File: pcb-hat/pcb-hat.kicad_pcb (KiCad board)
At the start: 4 copper layers, 40.9 x 60.1 mm, 67 parts, among them Q1 Q_PMOS_GSD, Q2 Q_NPN, Q3 PJA3404A_R1_00001, U1 Headers, U2 INA219AxD, U3 HTD Servo, U4 TL431DBZ, U5 AP63301WU-7, U7 AP63301WU-7, U8 Raspberry_Pi_Generic

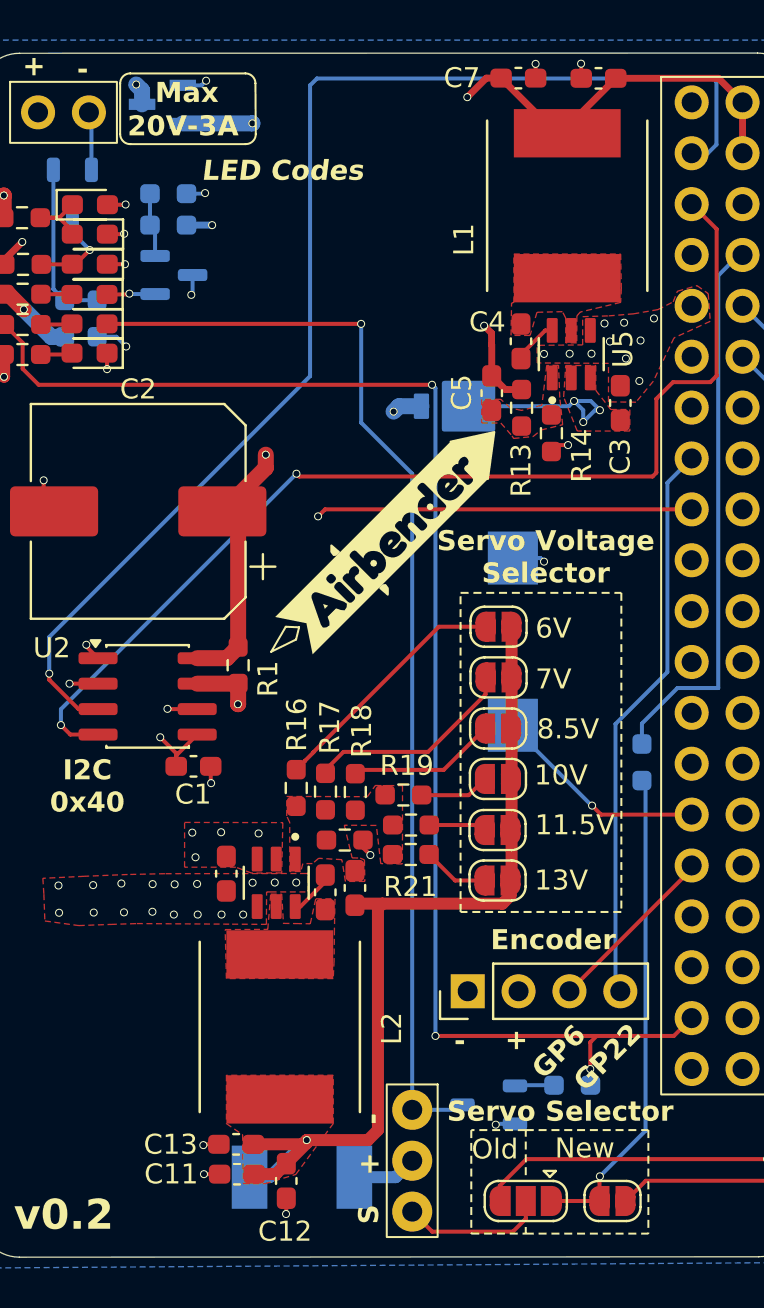
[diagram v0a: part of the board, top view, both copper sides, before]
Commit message: Add digikey pn's to caps and resistors, order board
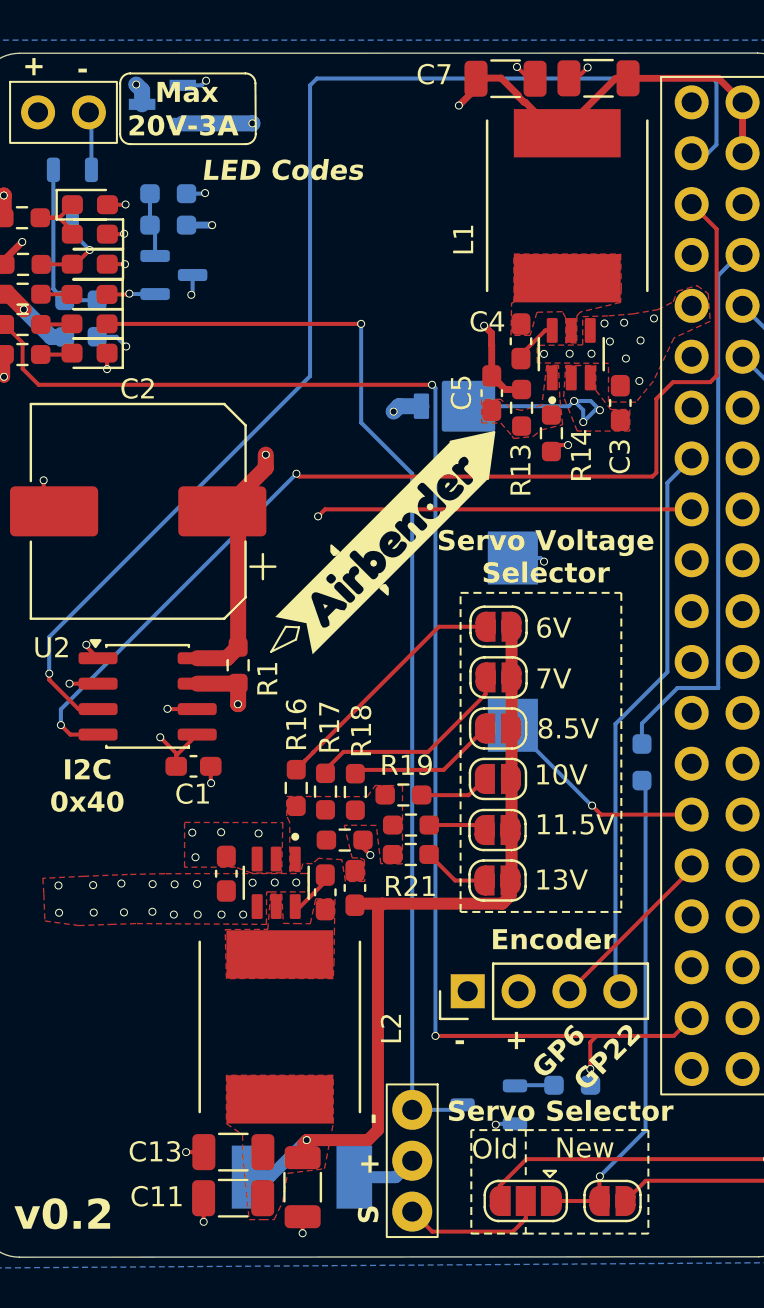
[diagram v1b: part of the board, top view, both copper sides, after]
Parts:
- C11, C12, C13, C6, C7: footprint Capacitor_SMD:C_0603_1608Metric_Pad1.08x0.95mm_HandSolder -> Capacitor_SMD:C_1206_3216Metric
- R17: value 233k -> 232k
- R19: value 346k -> 348k
- R20: value 403k -> 402k
- moved C11 1.21 mm to (123.8, 120.2)
- moved C12 0.87 mm to (127.3, 119.6)
- moved C7 0.64 mm to (137.4, 64.3)
- moved C13 0.41 mm to (123.8, 117.9)
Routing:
- net VDC: track 98.5 -> 92.8 mm
- net GND: track 24.6 -> 26.8 mm

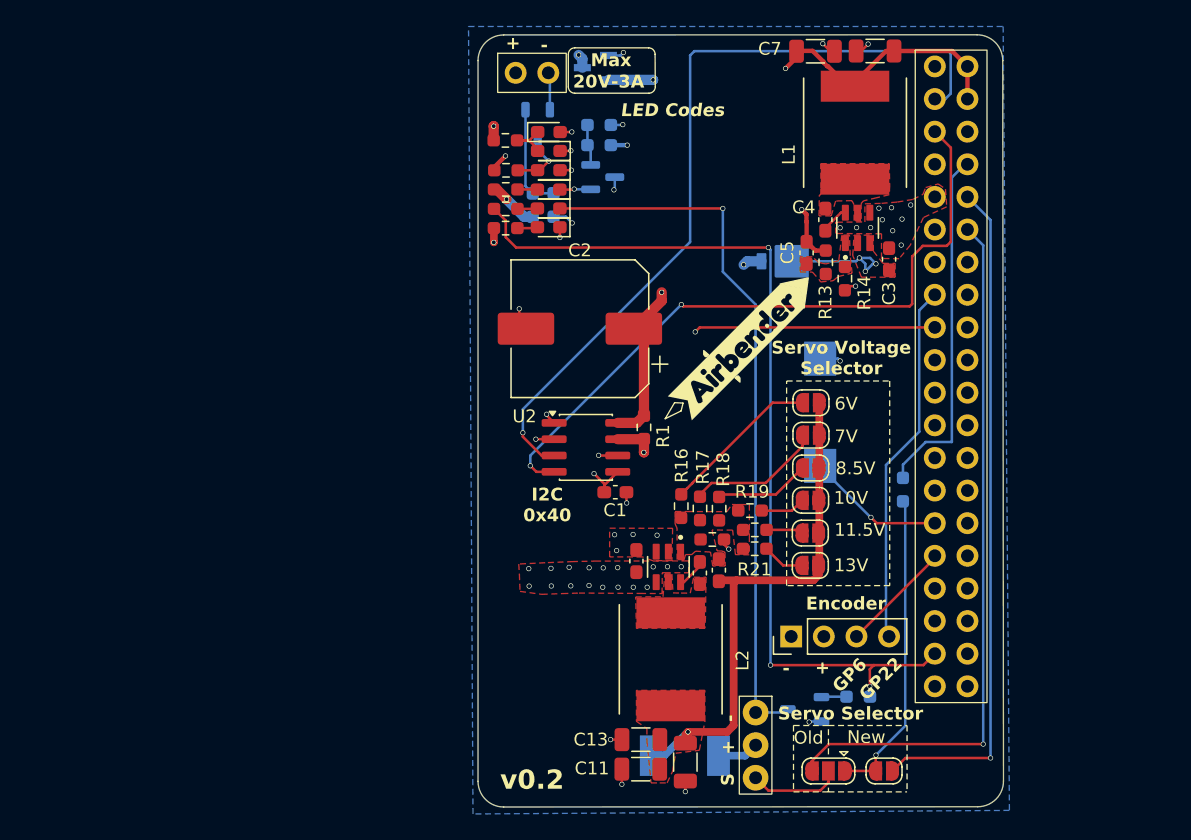
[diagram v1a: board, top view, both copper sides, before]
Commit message: Fix servo RP detection circuit
Start work on routing
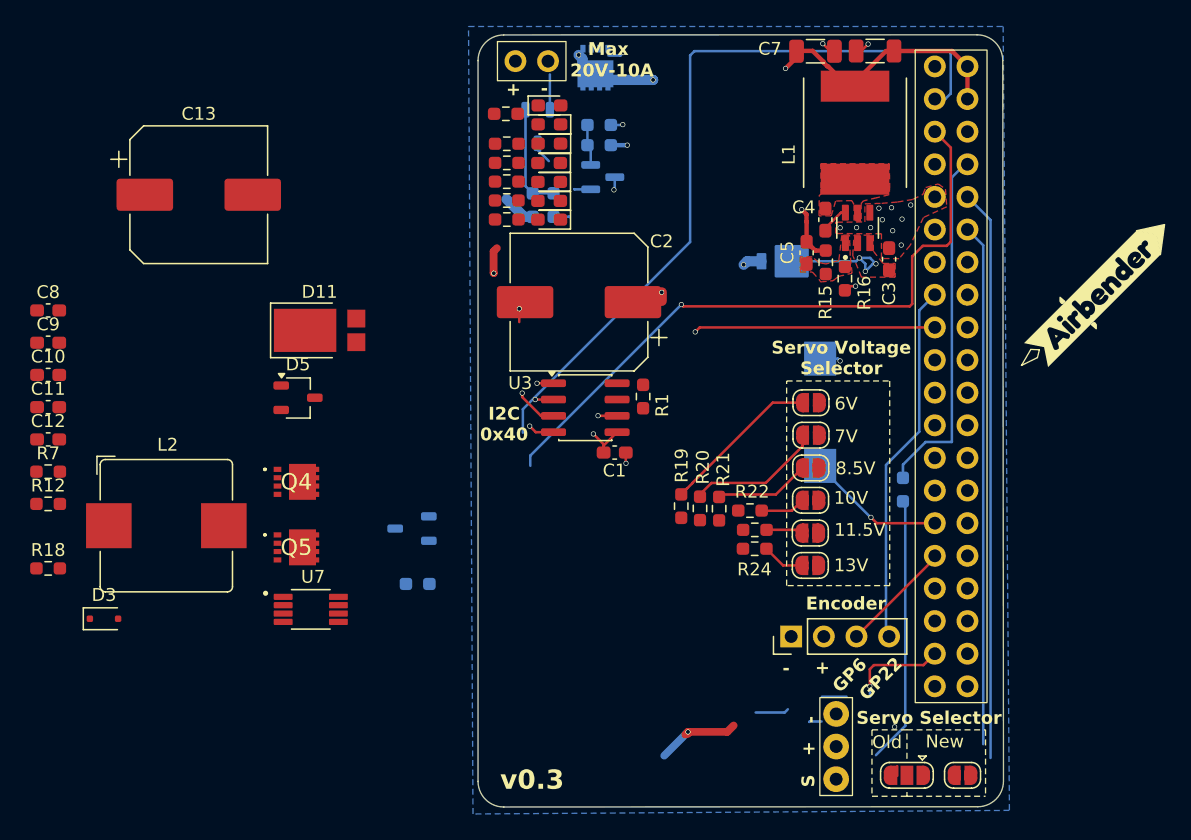
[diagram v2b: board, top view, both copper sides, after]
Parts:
- removed F1: 1812L110_24DR, pcb_hat:FUSM4632X200N
- removed the R15 at (129.4, 102.3)
- added D10: LED_Small, LED_SMD:LED_0603_1608Metric_Pad1.05x0.95mm_HandSolder, F.Cu at (116.7, 75.9)
- added D11: Schottky, Diode_SMD:D_PowerDI-5, F.Cu at (98.8, 86.0)
- added D3: TVS Diode, Diode_SMD:D_SOD-323F, F.Cu at (82.0, 108.5)
- added D5: Zener diode, Package_TO_SOT_SMD:TSOT-23, F.Cu at (97.1, 91.3)
- added Q4: Q_PMOS_GSD, pcb_hat:PJQ4465APAU_R2_000A1, F.Cu at (97.0, 97.8)
- added Q5: Q_PMOS_GSD, pcb_hat:PJQ4465APAU_R2_000A1, F.Cu at (97.0, 102.9)
- added R12: 10k, Resistor_SMD:R_0603_1608Metric_Pad0.98x0.95mm_HandSolder, F.Cu at (77.7, 99.5)
- added R17: 1k, Resistor_SMD:R_0603_1608Metric_Pad0.98x0.95mm_HandSolder, F.Cu at (113.4, 75.9)
- added R18: 49.9k, Resistor_SMD:R_0603_1608Metric_Pad0.98x0.95mm_HandSolder, F.Cu at (77.7, 104.5)
- added R7: 1k, Resistor_SMD:R_0603_1608Metric_Pad0.98x0.95mm_HandSolder, F.Cu at (77.7, 97.0)
- C10: value 12p -> 22u
- C11: value 22u -> 100p; footprint Capacitor_SMD:C_1206_3216Metric -> Capacitor_SMD:C_0603_1608Metric_Pad1.08x0.95mm_HandSolder
- C12: footprint Capacitor_SMD:C_1206_3216Metric -> Capacitor_SMD:C_0603_1608Metric_Pad1.08x0.95mm_HandSolder
- C13: value 22u -> 1000u; footprint Capacitor_SMD:C_1206_3216Metric -> Capacitor_SMD:CP_Elec_10x10.5
- C9: value 100n -> 22u
- L2: value 6.8u -> 4.7u; footprint pcb_hat:IND_ETQP4M6R8KVK -> Inductor_SMD:L_Bourns_SRP1038C_10.0x10.0mm
- Q1: footprint pcb_hat:SOT_7DS-T1-GE3_VIS -> pcb_hat:PJQ4465APAU_R2_000A1
- R14: renamed from R11; value 1k -> 2k
- R19: renamed from R16; value 196k -> 13k
- R20: renamed from R17; value 232k -> 10.7k
- R21: renamed from R18; value 290k -> 8.45k
- R22: renamed from R19; value 348k -> 6.98k
- R23: renamed from R20; value 402k -> 6.04k
- R24: renamed from R21; value 459k -> 5.23k
- R3: renamed from R6; value 4k7 -> 2k
- U7: value AP63301WU-7 -> LM3489; footprint pcb_hat:SOT95P280X100-6N -> pcb_hat:SOP65P490X110-8N
- moved C12 55.6 mm to (77.7, 94.5), turned to 0 degrees
- moved C13 54.6 mm to (89.4, 75.5), turned to 0 degrees
- moved C10 54.4 mm to (77.7, 89.5), turned to 0 degrees
- moved C11 54.1 mm to (77.7, 92.0), turned to 0 degrees
- moved C9 53.8 mm to (77.7, 87.0), turned to 0 degrees
- moved C8 49.8 mm to (77.7, 84.5), turned to 0 degrees
- moved L2 40.6 mm to (86.9, 101.2), turned to 0 degrees
- moved R8 35.4 mm to (106.5, 105.8)
- moved Q3 33.7 mm to (106.0, 101.4)
- moved kibuzzard-694E41B7 28.0 mm to (159.3, 83.2)
- moved U7 28.0 mm to (98.1, 107.7), turned to 0 degrees
- moved U2 6.27 mm to (139.0, 118.4)
- moved JP1 6.12 mm to (148.9, 120.7)
- moved JP2 6.12 mm to (144.5, 120.7)
- moved C1 3.09 mm to (121.8, 95.5)
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- renumbered D3 to D4, D4 to D6, D5 to D7, D7 to D9, R9 to R10, R10 to R11, R12 to R13, R13 to R15, R14 to R16, R3 to R4, R4 to R5, R5 to R6, R7 to R8, R8 to R9, U3 to U2, U2 to U3
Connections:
- net /Pi_RX_Out renamed /PI_RX_OUT
- net /Pi_SCL renamed /PI_SCL
- net /Pi_SDA renamed /PI_SDA
- net /Pi_TX_Out renamed /PI_TX_OUT
- C10 pad 1: VDC -> VCC_LOAD
- C10 pad 2: /V_Choose -> GND
- C11 pad 2: GND -> /V_CHOOSE
- C9 pad 1: Net-(U7-BST) -> VCC_LOAD
- C9 pad 2: Net-(U7-SW) -> GND
- D9 pad 1: /Servo_Control -> GND
- JP2 pad 2: Net-(JP2-C) -> /PI_SIGNAL
- JP3 pad 2: VDC -> GND
- JP4 pad 2: VDC -> GND
- JP5 pad 2: VDC -> GND
- JP6 pad 2: VDC -> GND
- JP7 pad 2: VDC -> GND
- JP8 pad 2: VDC -> GND
- L2 pad 1: Net-(U7-SW) -> Net-(D11-K)
- Q1 pad 1: GND -> VCC
- Q1 pad 3: +BATT -> VCC
- Q3 pad 3: /Servo_Control -> Net-(Q3-D)
- R14 pad 1: /GPIO26 -> /SERVO_SWITCH
- R19 pad 1: /V_Choose -> /V_CHOOSE
- R20 pad 1: /V_Choose -> /V_CHOOSE
- R21 pad 1: /V_Choose -> /V_CHOOSE
- R22 pad 1: /V_Choose -> /V_CHOOSE
- R23 pad 1: /V_Choose -> /V_CHOOSE
- R24 pad 1: /V_Choose -> /V_CHOOSE
- U2 pad 1: /Servo_Control -> GND
- U2 pad 2: /Fuse_Out -> /SERVO_SWITCH
- U2 pad 3: Net-(JP2-C) -> /SERVO_SIGNAL
- U7 pad 1: /V_Choose -> VCC_LOAD
- U7 pad 2: VCC_LOAD -> GND
- U7 pad 3: VCC_LOAD -> unconnected-(U7-EN-Pad3)
- U7 pad 4: GND -> /V_CHOOSE
- U7 pad 5: Net-(U7-SW) -> GND
- U7 pad 6: Net-(U7-BST) -> GND
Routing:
- net /GPIO26: track 71.7 -> 7.71 mm, vias 3 -> 1
- net /Servo_Control: track 55.6 -> 0.00 mm, vias 1 -> 0
- net VCC_LOAD: track 68.8 -> 17.2 mm, vias 7 -> 1
- net VDC: track 92.8 -> 55.6 mm
- net /GPIO18: track 55.2 -> 41.3 mm, vias 1 -> 0
- net +5V: track 106.1 -> 94.6 mm, vias 4 -> 3
- net VCC: track 32.3 -> 22.1 mm, vias 2 -> 3
- net /PI_RX_OUT: track 52.5 -> 44.4 mm, vias 1 -> 0
- net Net-(JP2-C): track 7.02 -> 0.00 mm
- net GND: track 26.8 -> 22.1 mm, vias 49 -> 23
- net Net-(D1-K): track 3.74 -> 0.00 mm
- net Net-(JP1-B): track 24.1 -> 20.5 mm, vias 1 -> 0
- net /Fuse_Out: track 3.23 -> 0.00 mm
- net +3V3: track 58.3 -> 55.2 mm
- net Net-(D4-A): track 3.76 -> 1.22 mm, vias 1 -> 0
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- removed copper zone on F.Cu, net /V_Choose
- removed copper zone on F.Cu, net Net-(U7-SW)
- removed copper zone on F.Cu, net VCC_LOAD
- removed copper zone on F.Cu, net VDC
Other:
- board text added: "20V-10A"
- board text added: "v0.3"
- board text removed: "20V-3A"
- board text removed: "LED Codes"
- board text removed: "v0.2"

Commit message: Finish routing PCB
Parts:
- removed the C6 at (142.1, 64.3)
- removed the D5 at (97.1, 91.3)
- removed kibuzzard-694E41B7: G***, kibuzzard-694E41B7
- added C4: 1u, Capacitor_SMD:C_0603_1608Metric_Pad1.08x0.95mm_HandSolder, B.Cu at (113.4, 83.4)
- added G***: LOGO, pcb_hat:airbender_logo, F.Cu at (141.3, 96.9)
- added Q5: Q_NPN, Package_TO_SOT_SMD:TSOT-23, B.Cu at (113.4, 80.5)
- added R11: 10k, Resistor_SMD:R_0603_1608Metric_Pad0.98x0.95mm_HandSolder, B.Cu at (113.3, 84.9)
- added U4: INA180A1, Package_TO_SOT_SMD:SOT-23-5, B.Cu at (136.1, 120.9)
- C1, D3, Q4, R1, U3: moved to B.Cu
- C10, C12, C9: footprint Capacitor_SMD:C_0603_1608Metric_Pad1.08x0.95mm_HandSolder -> Capacitor_SMD:C_1206_3216Metric
- C8: value 10u -> 22u; footprint Capacitor_SMD:C_0603_1608Metric_Pad1.08x0.95mm_HandSolder -> Capacitor_SMD:C_1206_3216Metric
- R10: renamed from R7; moved to B.Cu
- R13: renamed from R12; moved to B.Cu
- R18: renamed from R17; value 1k -> 2k
- R3: value 2k -> 4k7
- moved C8 63.2 mm to (137.6, 64.4)
- moved R10 62.1 mm to (136.0, 118.4), turned to 180 degrees
- moved R13 55.4 mm to (131.4, 113.3), turned to 180 degrees
- moved D3 55.0 mm to (137.0, 110.3), turned to 90 degrees
- moved C10 53.2 mm to (130.9, 87.4)
- moved C9 53.2 mm to (130.9, 85.1)
- moved C13 52.8 mm to (125.8, 113.7), turned to -135 degrees
- moved C12 50.3 mm to (126.8, 105.5), turned to 180 degrees
- moved C11 47.6 mm to (125.2, 95.5), turned to 90 degrees
- moved R19 46.9 mm to (123.7, 95.5), turned to 90 degrees
- moved L2 44.3 mm to (131.1, 99.1), turned to -90 degrees
- moved D10 36.9 mm to (135.4, 90.1), turned to 90 degrees
- moved Q4 36.6 mm to (131.7, 109.4), turned to 90 degrees
- moved Q6 36.3 mm to (131.1, 90.6)
- moved U8 31.9 mm to (126.0, 92.1)
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- renumbered C4 to C5, C5 to C6, D11 to D10, D6 to D5, D7 to D6, D8 to D7, D9 to D8, D10 to D9, Q5 to Q6, R11 to R12, R13 to R14, R14 to R15, R15 to R16, R16 to R17, R18 to R19, R19 to R20, R20 to R21, R21 to R22, R22 to R23, R23 to R24, R24 to R25, R8 to R7, R9 to R8, R10 to R9, U4 to U5, U5 to U6, U6 to U7, U7 to U8, U8 to U9
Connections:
- C8 pad 1: VCC_LOAD -> +5V
- D10 pad 1: Net-(D11-K) -> Net-(D10-K)
- D9 pad 1: GND -> Net-(D9-K)
- D9 pad 2: Net-(D10-A) -> +5V
- L2 pad 1: Net-(D11-K) -> Net-(D10-K)
- Q1 pad 9: (no net) -> +BATT
- Q4 pad 9: (no net) -> /SERVO_SWITCH
- Q6 pad 5: Net-(D11-K) -> Net-(D10-K)
- Q6 pad 6: Net-(D11-K) -> Net-(D10-K)
- Q6 pad 7: Net-(D11-K) -> Net-(D10-K)
- Q6 pad 8: Net-(D11-K) -> Net-(D10-K)
- Q6 pad 9: (no net) -> Net-(D10-K)
- R18 pad 1: /SERVO_RP_LED -> Net-(Q5-C)
- R18 pad 2: Net-(D10-A) -> Net-(D9-K)
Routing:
- net Net-(R11-Pad1): track 0.00 -> 58.1 mm, vias 0 -> 2
- net /SERVO_SWITCH: track 0.00 -> 52.7 mm, vias 0 -> 1
- net +5V: track 94.6 -> 130.2 mm
- net /PI_SDA: track 63.2 -> 31.8 mm, vias 1 -> 0
- net +3V3: track 55.2 -> 85.3 mm, vias 2 -> 3
- net /PI_SCL: track 53.8 -> 28.9 mm, vias 2 -> 0
- net GND: track 22.1 -> 46.9 mm, vias 23 -> 53
- net VCC: track 22.1 -> 0.00 mm, vias 3 -> 15
- net /PI_SIGNAL: track 0.00 -> 14.2 mm, vias 0 -> 3
- net /SERVO_SIGNAL: track 0.00 -> 13.1 mm, vias 0 -> 1
- net +BATT: track 0.00 -> 12.4 mm, vias 0 -> 3
- net VDC: track 55.6 -> 67.7 mm, vias 2 -> 8
- net Net-(JP3-A): track 12.4 -> 2.08 mm
- net Net-(JP4-A): track 10.4 -> 2.46 mm
- net /GPIO5: track 10.7 -> 3.11 mm, vias 1 -> 0
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- added copper zone on B.Cu, net /SERVO_SWITCH
- added copper zone on F.Cu, net /V_CHOOSE
- added copper zone on F.Cu, net Net-(D10-K)
- added copper zone on B.Cu, net VCC
- added copper zone on F.Cu, net VCC
- added copper zone on In2.Cu, net VCC
- added copper zone on B.Cu, net VCC_LOAD
- added copper zone on F.Cu, net VCC_LOAD
- added copper zone on In2.Cu, net VCC_LOAD
- added copper zone on B.Cu, net VDC
- added copper zone on F.Cu, net VDC
- added copper zone on In2.Cu, net VDC
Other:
- board text added: "Buzzer: GPIO 5 ▲ Servo: GPIO 26 ▲"
- board text added: "E N C"
- board text added: "PWM"
- board text added: "Servo Selector"
- board text added: "UART"
- board text removed: "Buzzer"
- board text removed: "Drive GPIO 5 High"
- board text removed: "Encoder"
- board text removed: "New"
- board text removed: "Old"
